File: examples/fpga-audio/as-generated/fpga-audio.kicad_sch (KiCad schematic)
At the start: 29 parts, among them J1 3V3 IN, J2 AUDIO OUT, J3 SPI PROG, U1 iCE40UP5K, U2 PCM5102A, U3 AP2112K-1.2, U4 W25Q32JV, X1 12MHz

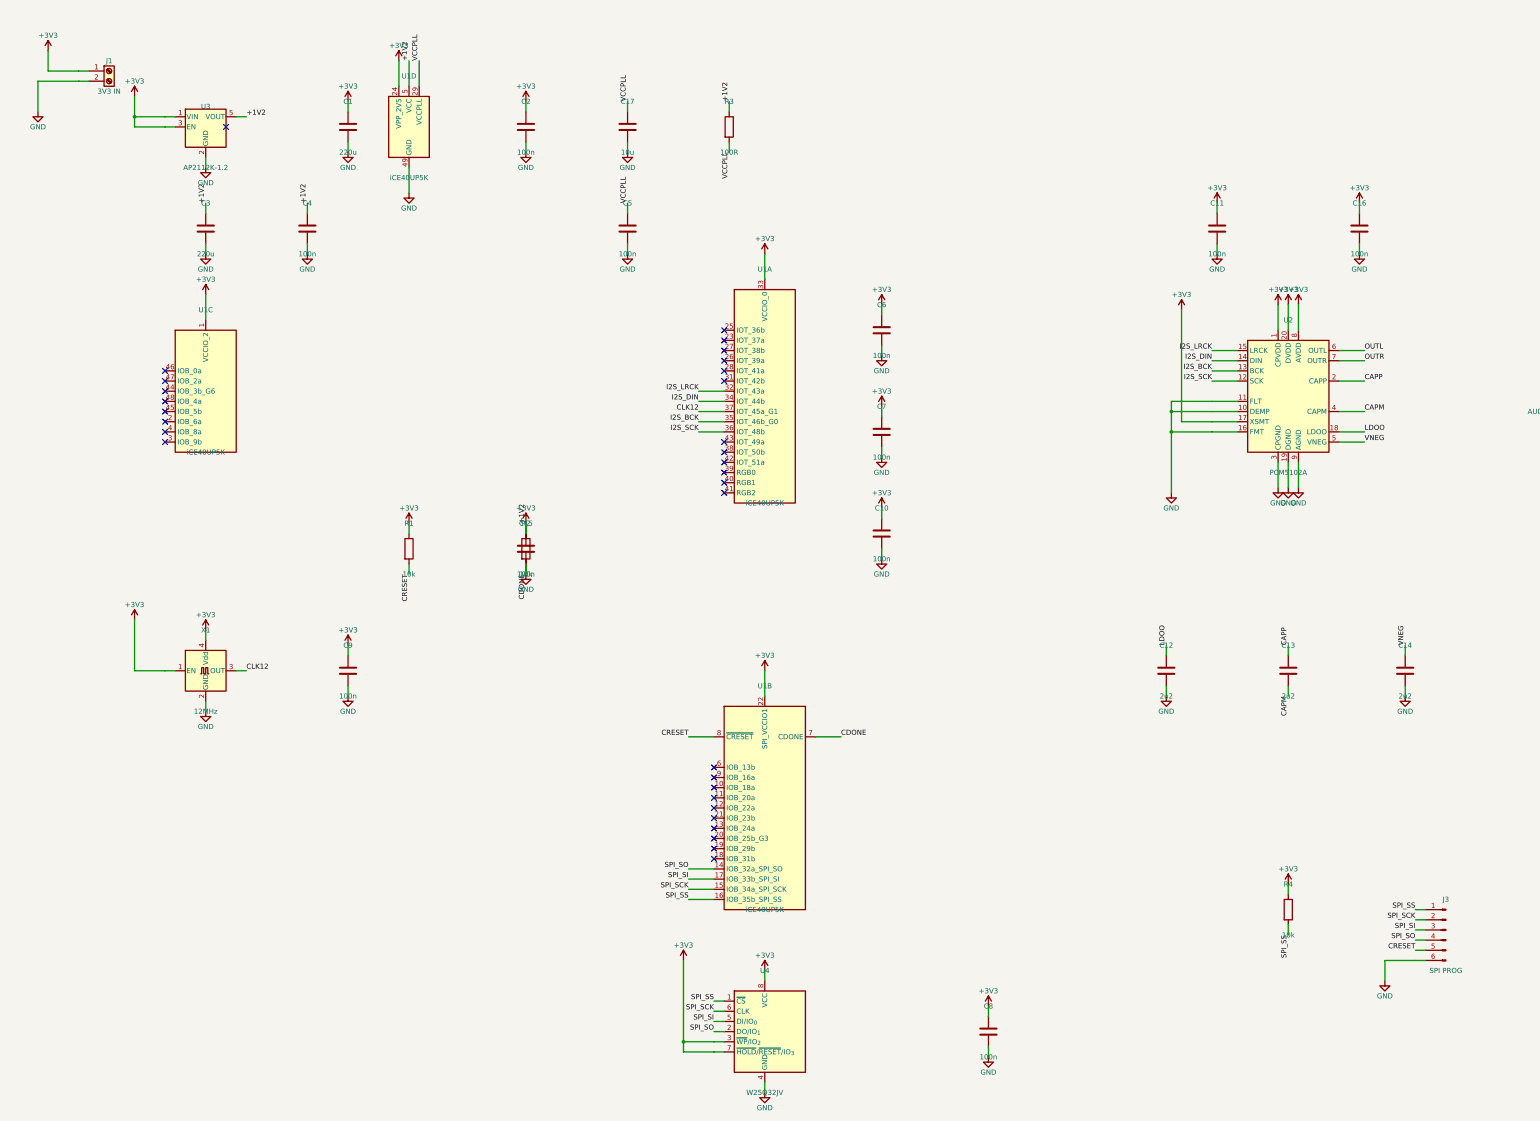
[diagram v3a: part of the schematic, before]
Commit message: Gather the FPGA sheet into blocks
Power, clock, config and codec each draw together with their own note
beside them, in place of parts spread over the whole of an A3 with
every net crossing the gap. The programming header comes off the title
block and the two long notes come back inside the frame.

Co-Authored-By: Claude Fable 5 <noreply@anthropic.com>
Claude-Session: https://claude.ai/code/session_01DUj7Ltu92tWg159mCSacwY
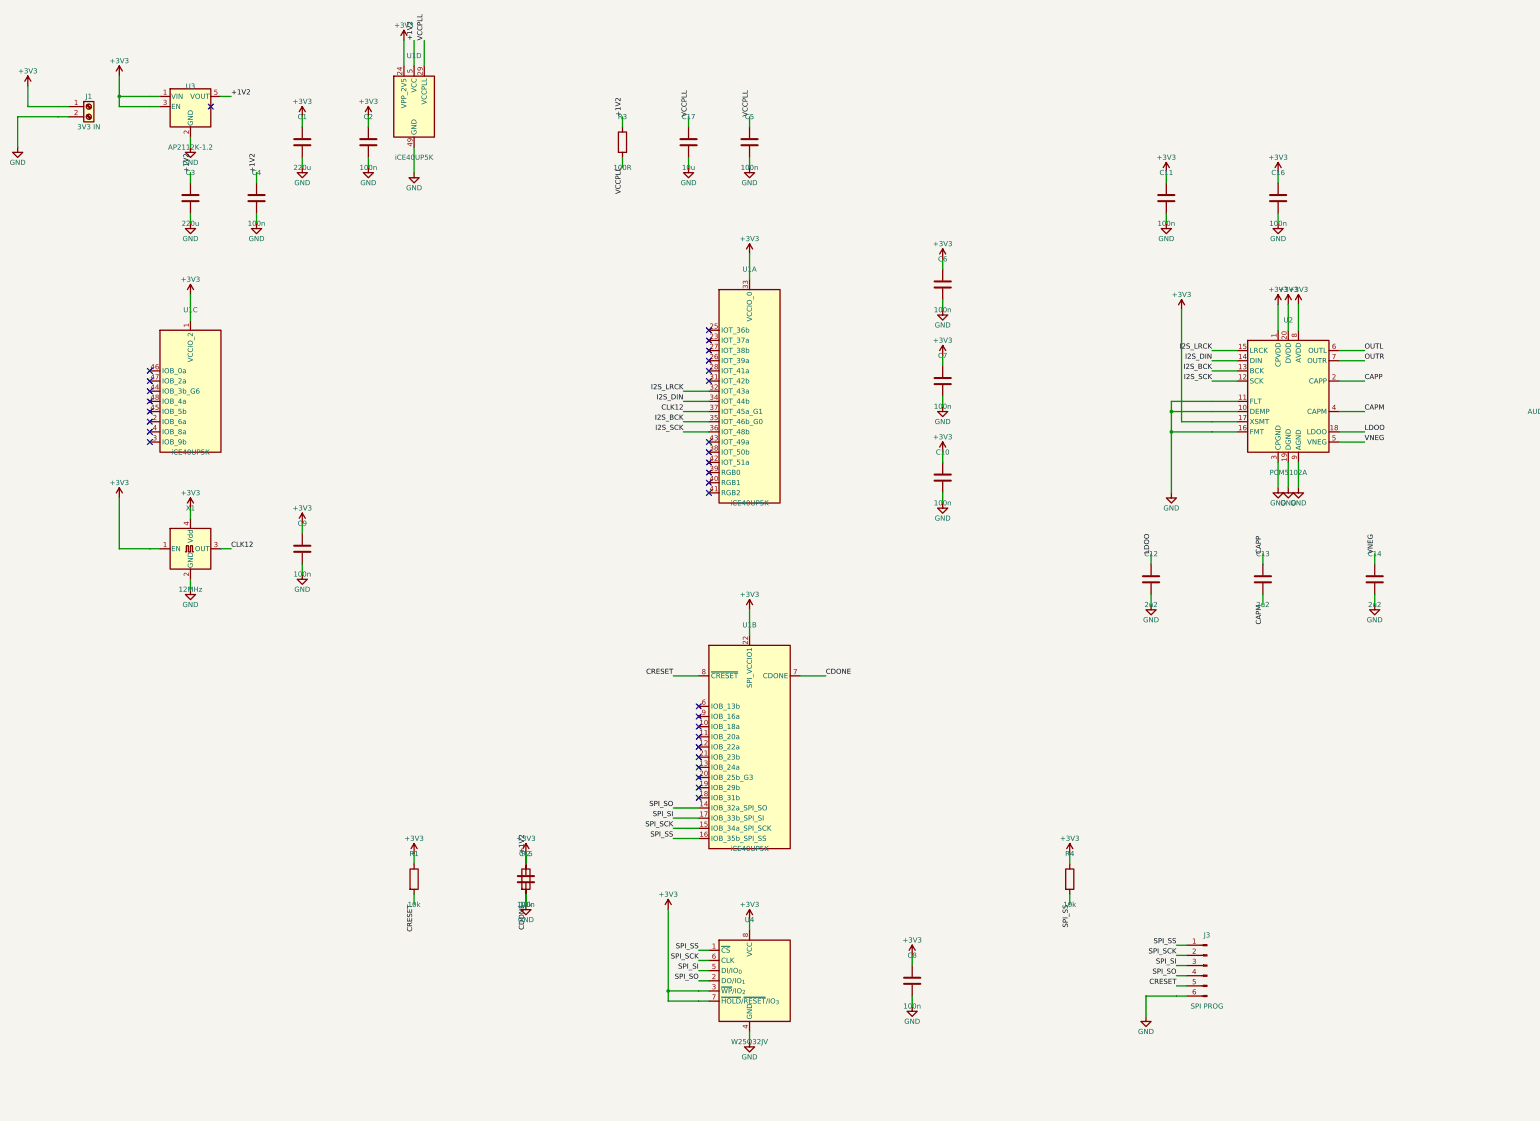
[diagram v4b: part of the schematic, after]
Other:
- moved on the sheet: C1, C10, C11, C12, C13, C14, C15, C16, C17, C2, C3, C4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
